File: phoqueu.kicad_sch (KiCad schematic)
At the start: 54 parts, among them J1 18…56 V, J2 On / Off, J3 3.3…24 V, Q1 SiR120DP, Q2 SiR120DP, Q3 SiR120DP, Q4 SiR120DP, SW1 Remote, SW2 Voltage select, T1 320 µ, T2 180 µ, U1 LT4320, U2 i7A4W033A033V

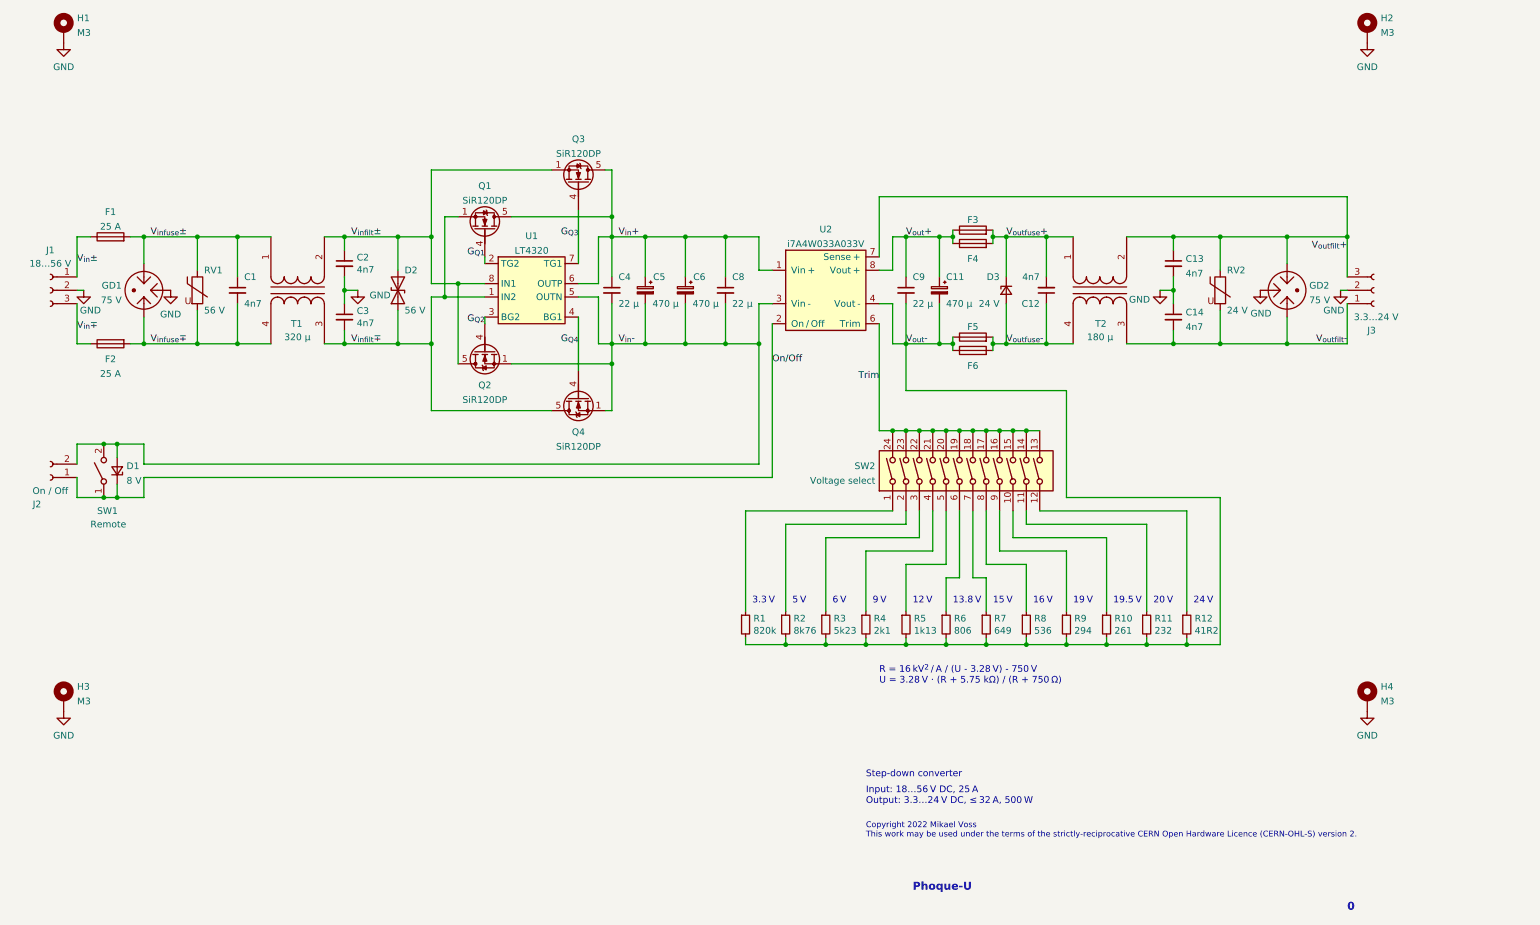
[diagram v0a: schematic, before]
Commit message: Revise schematic
- Remove remote on/off connector,
- remove extra fuses,
- adjust overvoltage protection values,
- replace switches with pin headers,
- replace input and output power connectors,
- add microcontroller for supervision,
- add hall‐effect current sensors,
- adjust electrolytic capacitors,
- remove output common‐mode choke,
- adjust filter capacitors,
- remove rectifier circuit,
- add varistors to limit earth potentials.
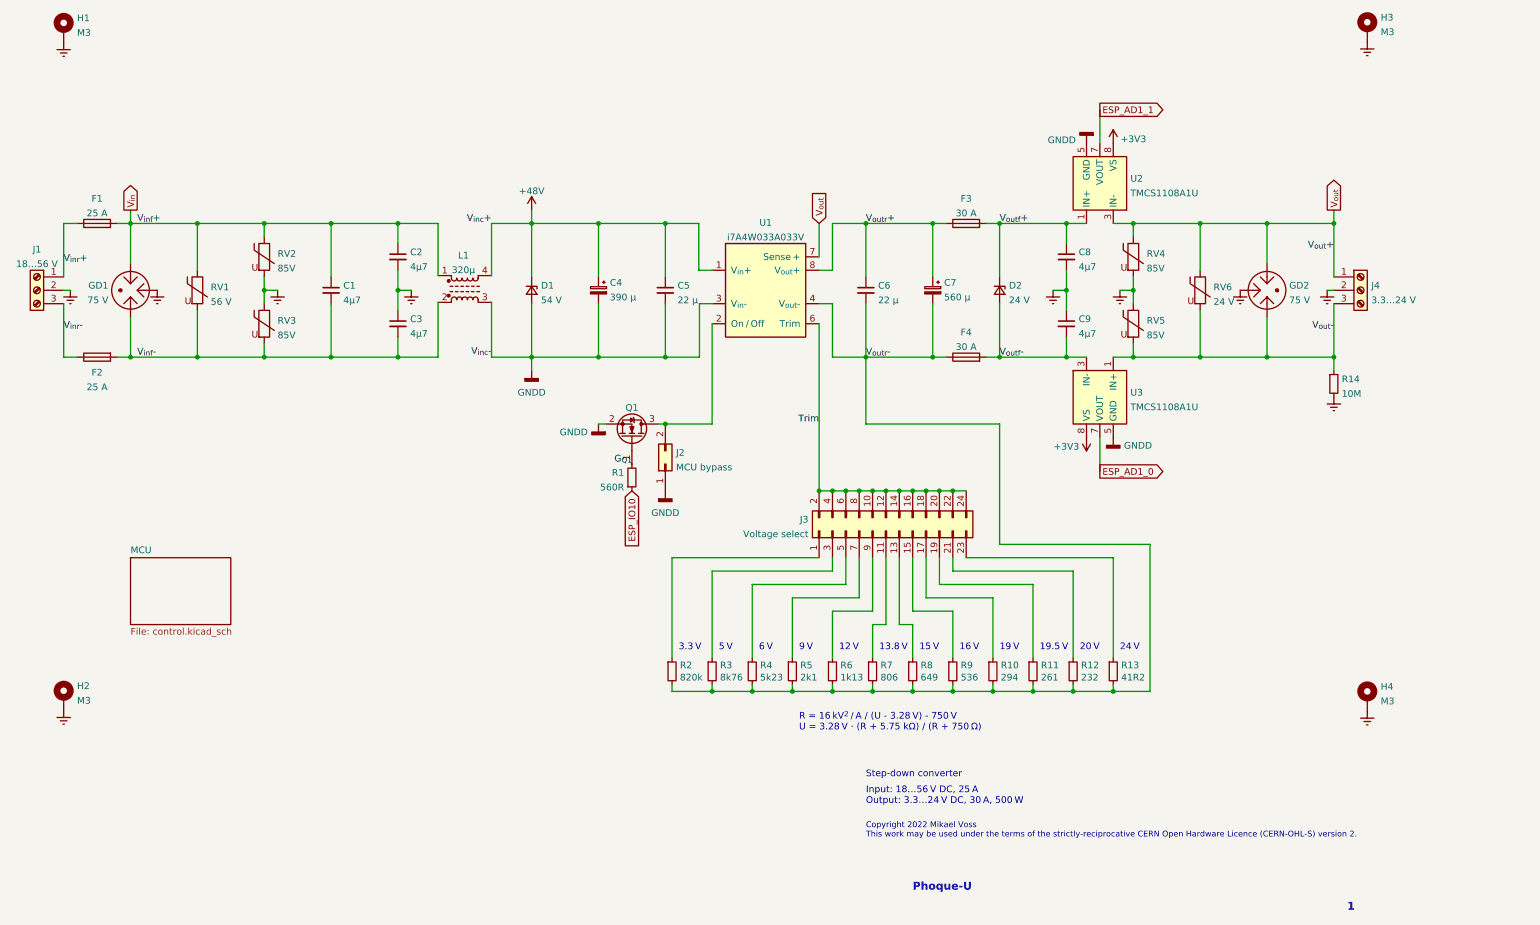
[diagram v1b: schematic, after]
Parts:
- removed C11, C5: 470 µ, Local:CP_Radial_D16.0mm_P7.50mm, symbol Device:C_Polarized_Small
- removed C12, C13, C14: 4n7, Local:C_Disc_D13mm_W6.0mm_P10.00mm, symbol Device:C_Small
- removed C4: 22 µ, Local:KRM55WR71J226MH01, symbol Device:C_Small
- removed D1: 8 V, Diode_SMD:D_SMF, symbol Device:D_Zener_Small
- removed F4, F6: ≤ 32 A, Local:8040, symbol Device:Fuse
- removed J2: On / Off, Local:2604-1102, symbol Connector:Conn_01x02_Female
- removed Q1, Q2, Q3, Q4: SiR120DP, Package_SO:Vishay_PowerPAK_1212-8_Single, symbol Local:SiR120DP
- removed SW1: Remote, Local:418127160901, symbol Switch:SW_SPST
- removed SW2: Voltage select, Local:418127160912, symbol Switch:SW_DIP_x12
- removed T1: 320 µ, Local:CMX1211Z321B-10, symbol Device:Transformer_1P_1S
- removed T2: 180 µ, Local:CMX1211Z181B-10, symbol Device:Transformer_1P_1S
- removed U1: LT4320, Package_DFN_QFN:DFN-8-1EP_3x3mm_P0.5mm_EP1.65x2.38mm, symbol Local:LT4320
- added C7: 560 µ, Capacitor_THT:C_Radial_D10.0mm_H20.0mm_P5.00mm, symbol Device:C_Polarized_Small
- added C8, C9: 4µ7, Capacitor_SMD:C_1210_3225Metric, symbol Device:C_Small
- added J2: MCU bypass, Connector_PinHeader_2.54mm:PinHeader_2x01_P2.54mm_Vertical, symbol Connector_Generic:Conn_02x01
- added J3: Voltage select, Connector_PinHeader_2.54mm:PinHeader_2x12_P2.54mm_Vertical, symbol Connector_Generic:Conn_02x12_Odd_Even
- added L1: 320µ, phq_SMD:CMX1211Z321B-10, symbol Device:L_Ferrite_Coupled_1423
- added Q1: NX138AK, Package_TO_SOT_SMD:SOT-23, symbol Device:Q_NMOS_GSD
- added R1: 560R, Resistor_SMD:R_0805_2012Metric, symbol Device:R_Small
- added R14: 10M, Resistor_SMD:R_0805_2012Metric, symbol Device:R_Small
- added RV3, RV4, RV5: 85V, Capacitor_SMD:C_1206_3216Metric, symbol Device:Varistor
- added RV6: 24 V, Capacitor_SMD:C_1210_3225Metric, symbol Device:Varistor
- added U2, U3: TMCS1108A1U, Package_SO:SOIC-8_3.9x4.9mm_P1.27mm, symbol phq_IC:TMCS1108A1U
- C1: value 4n7 -> 4µ7; footprint Local:C_Disc_D13mm_W6.0mm_P10.00mm -> Capacitor_SMD:C_1210_3225Metric; Manufacturer (none) -> Kyocera AVX; Part Number CD45-E2GA472M-NKA -> 12101C475K4T2A
- C2, C3: value 4n7 -> 4µ7; footprint Local:C_Disc_D13mm_W6.0mm_P10.00mm -> Capacitor_SMD:C_1210_3225Metric
- C4: renamed from C6; value 470 µ -> 390 µ; footprint Local:CP_Radial_D16.0mm_P7.50mm -> Capacitor_THT:C_Radial_D12.5mm_H20.0mm_P5.00mm; Manufacturer (none) -> Nichicon; Part Number URZ1J471MHD -> UHW1J391MHD6
- C5: renamed from C8; footprint Local:KRM55WR71J226MH01 -> Capacitor_SMD:C_2220_5650Metric; Manufacturer (none) -> Murata; Part Number KRM55WR71J226MH01K -> KRM55WR72A226MH01L
- C6: renamed from C9; footprint Local:KRM55WR71J226MH01 -> Capacitor_SMD:C_2220_5650Metric; Manufacturer (none) -> Murata
- D1: renamed from D2; value 56 V -> 54 V; footprint Local:D_BZW50-56B_P12.70mm_Horizontal -> Diode_SMD:D_SMB; symbol Device:D_TVS -> Device:D_Zener_Small; Manufacturer (none) -> Bourns; Part Number BZW50-56B -> 1.5SMBJ54A-H
- D2: renamed from D3; footprint Diode_SMD:D_SMC -> Diode_SMD:D_SMA; Manufacturer (none) -> STMicroelectronics; Part Number SMC30J24A -> SMA6F24A
- F1, F2: footprint Local:3557 -> phq_THT:Keystone 3557
- F3: value ≤ 32 A -> 30 A; footprint Local:3557 -> phq_THT:Keystone 3557
- F4: renamed from F5; value ≤ 32 A -> 30 A; footprint Local:3557 -> phq_THT:Keystone 3557
- GD1, GD2: footprint Local:2036-NN-SM -> phq_SMD:2036-NN-SM; Manufacturer (none) -> Bourns
- J1: footprint Local:2606-1103 -> (none); symbol Connector:Conn_01x03_Female -> Connector:Screw_Terminal_01x03; Part Number 2606-1103 -> (none)
- J4: renamed from J3; footprint Local:2606-1103 -> (none); symbol Connector:Conn_01x03_Female -> Connector:Screw_Terminal_01x03; Part Number 2606-1103 -> (none)
- RV1: footprint Resistor_SMD:R_0805_2012Metric -> Capacitor_SMD:C_2220_5650Metric; Manufacturer (none) -> TDK
- RV2: value 24 V -> 85V; footprint Resistor_SMD:R_0805_2012Metric -> Capacitor_SMD:C_1206_3216Metric; Manufacturer (none) -> Bourns; Part Number B72530T6170K062 -> ZV60K1206121NIR1
- U1: renamed from U2; footprint Local:i7A4W033A033V-0C1 -> phq_Module:i7A4W-001; symbol Local:i7A4W033A033V -> phq_Module:i7A4W033A033V-0C1
- renumbered H3 to H2, H2 to H3, R9 to R10, R10 to R11, R11 to R12, R12 to R13, R1 to R2, R2 to R3, R3 to R4, R4 to R5, R5 to R6, R6 to R7, R7 to R8, R8 to R9
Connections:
- net V_{in}+ is gone; now on net +48V: C4.1, C5.1, U1.1 (V_{in}+)
- net V_{in}- is gone; now on net GNDD: C4.2, C5.2, U1.3 (V_{in}-)
- net G_{Q1}: now also Q1.1 (G), R1.2
- net Trim: now also J3.10 (Pin_10), J3.12 (Pin_12), J3.14 (Pin_14), J3.16 (Pin_16), J3.18 (Pin_18), J3.2 (Pin_2), J3.20 (Pin_20), J3.22 (Pin_22), J3.24 (Pin_24), J3.4 (Pin_4), J3.6 (Pin_6), J3.8 (Pin_8)
- net V_{out}-: now also GD2.1, J4.3 (Pin_3), R14.1, RV5.2, RV6.2, U3.1 (IN+), U3.2 (IN+); no longer C6.2, F4.1, R10.2, R11.2, R12.2, R13.2, R2.2, R3.2, R4.2, R5.2, R6.2, R7.2, R8.2, R9.2, U1.4 (Vout -)
- net at R2.1: now also J3.1 (Pin_1)
- net at R3.1: now also J3.3 (Pin_3)
- net at R4.1: now also J3.5 (Pin_5)
- net at R5.1: now also J3.7 (Pin_7)
- net at R6.1: now also J3.9 (Pin_9)
- net at R7.1: now also J3.11 (Pin_11)
- net at R10.1: now also J3.17 (Pin_17)
- net at R11.1: now also J3.19 (Pin_19)
- net at R12.1: now also J3.21 (Pin_21)
- net at R13.1: now also J3.23 (Pin_23)
- net at R8.1: now also J3.13 (Pin_13)
- net at R9.1: now also J3.15 (Pin_15)
- net GND renamed Earth
- net Earth: now also RV2.2, C8.2, C9.1, R14.2, RV3.1, RV4.2, RV5.1
- net On/Off: no longer names the net of U1.2 (On / Off)
- net On/Off: now also J2.2 (Pin_2), Q1.3 (D)
- net V_{infilt}± renamed GNDD
- net GNDD: now also J2.1 (Pin_1), L1.3, Q1.2 (S), U2.5 (GND), U2.6 (NC), U3.5 (GND), U3.6 (NC); no longer C2.1
- net V_{infilt}∓ renamed +48V
- net +48V: now also L1.4; no longer C3.2
- net V_{infuse}± renamed V_{in}
- net V_{in}: now also C2.1, RV2.1, L1.1
- net V_{infuse}∓ renamed V_{inf}-
- net V_{inf}-: now also C3.2, L1.2, RV3.2
- net V_{in}± renamed V_{inr}+
- net V_{in}∓ renamed V_{inr}-
- net V_{outfilt}+ renamed V_{out}
- net V_{out}: now also J4.1 (Pin_1), RV4.1, RV6.1, U2.3 (IN-), U2.4 (IN-); no longer J4.3 (Pin_3), RV2.1
- removed net V_{outfilt}-: GD2.1, J4.1 (Pin_1), RV2.2
- net V_{outfuse}+ renamed V_{outf}+
- net V_{outf}+: now also C8.1, U2.1 (IN+), U2.2 (IN+)
- net V_{outfuse}- renamed V_{outf}-
- net V_{outf}-: now also C9.2, U3.3 (IN-), U3.4 (IN-)
- net V_{out}+ renamed V_{outr}+
- net V_{outr}+: now also C7.1
- new net +3V3: U2.8 (VS), U3.8 (VS)
- new net ESP_AD1_0: U3.7 (VOUT)
- new net ESP_AD1_1: U2.7 (VOUT)
- new net ESP_IO10: R1.1
- new net V_{outr}-: C6.2, C7.2, F4.1, R10.2, R11.2, R12.2, R13.2, R2.2, R3.2, R4.2, R5.2, R6.2, R7.2, R8.2, R9.2, U1.4 (V_{out}-)
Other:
- added sheet MCU (control.kicad_sch)
- note added: "1"
- note added: "Input: 18…56 V DC, 25 A Output: 3.3…24 V DC, 30 A, 500 W"
- note removed: "0"
- note removed: "Input: 18…56 V DC, 25 A Output: 3.3…24 V DC, ≤ 32 A, 500 W"
- moved on the sheet: C1, C2, C3, C4, C5, C6, D1, D2, F1, F2, F3, F4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

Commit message: Complete footprint assignments
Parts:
- C4: footprint Capacitor_THT:C_Radial_D12.5mm_H20.0mm_P5.00mm -> Capacitor_THT:CP_Radial_D12.5mm_P5.00mm
- C7: footprint Capacitor_THT:C_Radial_D10.0mm_H20.0mm_P5.00mm -> Capacitor_THT:CP_Radial_D10.0mm_P5.00mm
- F1, F2, F3, F4: footprint phq_THT:Keystone 3557 -> phq_THT:Keystone_3557
- J1, J4: footprint (none) -> phq_Connector:Phoenix_1987737
- U1: footprint phq_Module:i7A4W-001 -> phq_Module:i7A4W-0C1
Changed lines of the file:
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@@
     (property "Reference" "J1" (id 0) (at 20.32 68.4235 0))
     (property "Value" "18…56 V" (id 1) (at 20.32 71.1986 0))
-    (property "Footprint" "" (id 2) (at 20.32 76.2 0)
+    (property "Footprint" "phq_Connector:Phoenix_1987737" (id 2) (at 20.32 76.2 0)
       (effects (font (size 1.27 1.27)) hide)
     )
@@
     (property "Reference" "F1" (id 0) (at 31.75 58.7715 90))
     (property "Value" "25 A" (id 1) (at 31.75 61.5466 90))
-    (property "Footprint" "phq_THT:Keystone 3557" (id 2) (at 31.75 65.278 90)
+    (property "Footprint" "phq_THT:Keystone_3557" (id 2) (at 31.75 65.278 90)
       (effects (font (size 1.27 1.27)) hide)
     )
@@
       (effects (font (size 1.27 1.27)) (justify left))
     )
-    (property "Footprint" "" (id 2) (at 271.78 76.2 0)
+    (property "Footprint" "phq_Connector:Phoenix_1987737" (id 2) (at 271.78 76.2 0)
       (effects (font (size 1.27 1.27)) hide)
     )
@@
     (property "Reference" "U1" (id 0) (at 158.75 63.3435 0))
     (property "Value" "i7A4W033A033V" (id 1) (at 158.75 66.1186 0))
-    (property "Footprint" "phq_Module:i7A4W-001" (id 2) (at 158.75 62.23 0)
+    (property "Footprint" "phq_Module:i7A4W-0C1" (id 2) (at 158.75 62.23 0)
       (effects (font (size 1.27 1.27)) hide)
     )
@@
     (property "Reference" "F3" (id 0) (at 196.85 58.7715 90))
     (property "Value" "30 A" (id 1) (at 196.85 61.5466 90))
-    (property "Footprint" "phq_THT:Keystone 3557" (id 2) (at 196.85 65.278 90)
+    (property "Footprint" "phq_THT:Keystone_3557" (id 2) (at 196.85 65.278 90)
       (effects (font (size 1.27 1.27)) hide)
     )
@@
     (property "Reference" "F4" (id 0) (at 196.85 84.1715 90))
     (property "Value" "30 A" (id 1) (at 196.85 86.9466 90))
-    (property "Footprint" "phq_THT:Keystone 3557" (id 2) (at 196.85 90.678 90)
+    (property "Footprint" "phq_THT:Keystone_3557" (id 2) (at 196.85 90.678 90)
       (effects (font (size 1.27 1.27)) hide)
     )
@@
       (effects (font (size 1.27 1.27)) (justify right))
     )
-    (property "Footprint" "Capacitor_THT:C_Radial_D12.5mm_H20.0mm_P5.00mm" (id 2) (at 127 76.2 0)
+    (property "Footprint" "Capacitor_THT:CP_Radial_D12.5mm_P5.00mm" (id 2) (at 127 76.2 0)
       (effects (font (size 1.27 1.27)) hide)
     )
@@
       (effects (font (size 1.27 1.27)) (justify right))
     )
-    (property "Footprint" "Capacitor_THT:C_Radial_D10.0mm_H20.0mm_P5.00mm" (id 2) (at 190.5 76.2 0)
+    (property "Footprint" "Capacitor_THT:CP_Radial_D10.0mm_P5.00mm" (id 2) (at 190.5 76.2 0)
       (effects (font (size 1.27 1.27)) hide)
     )
@@
     (property "Reference" "F2" (id 0) (at 31.75 91.8115 90))
     (property "Value" "25 A" (id 1) (at 31.75 94.5866 90))
-    (property "Footprint" "phq_THT:Keystone 3557" (id 2) (at 31.75 87.122 90)
+    (property "Footprint" "phq_THT:Keystone_3557" (id 2) (at 31.75 87.122 90)
       (effects (font (size 1.27 1.27)) hide)
     )
@@
       (effects (font (size 1.27 1.27)) hide)
     )
-    (property "Datasheet" "" (id 3) (at 229.87 96.52 0)
+    (property "Datasheet" "https://www.ti.com/lit/ds/symlink/tmcs1108.pdf" (id 3) (at 229.87 96.52 0)
       (effects (font (size 1.27 1.27)) hide)
     )
@@
       (effects (font (size 1.27 1.27)) hide)
     )
-    (property "Datasheet" "" (id 3) (at 214.63 55.88 0)
+    (property "Datasheet" "https://www.ti.com/lit/ds/symlink/tmcs1108.pdf" (id 3) (at 214.63 55.88 0)
       (effects (font (size 1.27 1.27)) hide)
     )
@@
     )
     (path "/545dcca5-4516-4b56-930c-fa32800a5d09"
-      (reference "C4") (unit 1) (value "390 µ") (footprint "Capacitor_THT:C_Radial_D12.5mm_H20.0mm_P5.00mm")
+      (reference "C4") (unit 1) (value "390 µ") (footprint "Capacitor_THT:CP_Radial_D12.5mm_P5.00mm")
     )
     (path "/00000000-0000-0000-0000-000061de344a"
@@
     )
     (path "/706d5b5d-54d1-4269-9ccc-cbc4d1b6d1b1"
-      (reference "C7") (unit 1) (value "560 µ") (footprint "Capacitor_THT:C_Radial_D10.0mm_H20.0mm_P5.00mm")
+      (reference "C7") (unit 1) (value "560 µ") (footprint "Capacitor_THT:CP_Radial_D10.0mm_P5.00mm")
     )
     (path "/61409210-3cfd-4077-8aca-d85223ff9dd2"
@@
     )
     (path "/00000000-0000-0000-0000-000061cea85f"
-      (reference "F1") (unit 1) (value "25 A") (footprint "phq_THT:Keystone 3557")
+      (reference "F1") (unit 1) (value "25 A") (footprint "phq_THT:Keystone_3557")
     )
     (path "/87dcb324-6692-4a89-9fda-c691d148a6fa"
-      (reference "F2") (unit 1) (value "25 A") (footprint "phq_THT:Keystone 3557")
+      (reference "F2") (unit 1) (value "25 A") (footprint "phq_THT:Keystone_3557")
     )
     (path "/00000000-0000-0000-0000-000061f10d81"
-      (reference "F3") (unit 1) (value "30 A") (footprint "phq_THT:Keystone 3557")
+      (reference "F3") (unit 1) (value "30 A") (footprint "phq_THT:Keystone_3557")
     )
     (path "/00000000-0000-0000-0000-000061f20390"
-      (reference "F4") (unit 1) (value "30 A") (footprint "phq_THT:Keystone 3557")
+      (reference "F4") (unit 1) (value "30 A") (footprint "phq_THT:Keystone_3557")
     )
     (path "/b964d121-1ca9-4d94-9cd9-a72a5247427a/f629f221-7947-4a84-8e39-44b1090eabb8"
@@
     )
     (path "/00000000-0000-0000-0000-000061ce1fbe"
-      (reference "J1") (unit 1) (value "18…56 V") (footprint "")
+      (reference "J1") (unit 1) (value "18…56 V") (footprint "phq_Connector:Phoenix_1987737")
     )
     (path "/b48a8561-9da0-49f0-a478-043f03753e85"
@@
     )
     (path "/00000000-0000-0000-0000-000061d6d641"
-      (reference "J4") (unit 1) (value "3.3…24 V") (footprint "")
+      (reference "J4") (unit 1) (value "3.3…24 V") (footprint "phq_Connector:Phoenix_1987737")
     )
     (path "/b964d121-1ca9-4d94-9cd9-a72a5247427a/1fbd6f20-e054-41ef-8930-3ae35b267af3"
@@
     )
     (path "/b964d121-1ca9-4d94-9cd9-a72a5247427a/cb7151d5-e2ab-4025-b1e2-8bdcd9fdf752"
-      (reference "L2") (unit 1) (value "15µ") (footprint "")
+      (reference "L2") (unit 1) (value "15µ") (footprint "phq_SMD:WE-LQS_4018")
     )
     (path "/5726c03a-2dcc-427a-9a76-e9bc5e71ec3d"
@@
     )
     (path "/00000000-0000-0000-0000-000061e0f358"
-      (reference "U1") (unit 1) (value "i7A4W033A033V") (footprint "phq_Module:i7A4W-001")
+      (reference "U1") (unit 1) (value "i7A4W033A033V") (footprint "phq_Module:i7A4W-0C1")
     )
     (path "/c9871f6b-9c72-4b75-a42a-a5b6334526f5"
@@
     )
     (path "/b964d121-1ca9-4d94-9cd9-a72a5247427a/a392fef5-46e3-46d5-8624-fab661b9f6d6"
-      (reference "U5") (unit 1) (value "ESP32-C3-MINI-1U") (footprint "")
+      (reference "U5") (unit 1) (value "ESP32-C3") (footprint "phq_Module:ESP32-C3-MINI-1U")
     )
     (path "/b964d121-1ca9-4d94-9cd9-a72a5247427a/83a9ae57-3260-46c7-b00c-064feff08fc9"
